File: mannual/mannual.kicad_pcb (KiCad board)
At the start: 2 copper layers, 31 parts, among them J1 Conn_02x07_Odd_Even, J10 Conn_02x10_Odd_Even, J2 Conn_01x02, J3 Conn_01x02, J4 Conn_01x02, J5 Conn_01x02, J6 Conn_01x02, J7 Conn_01x02, J8 Conn_01x02, J9 Conn_02x10_Odd_Even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

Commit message: modified the automatic circuit
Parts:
- moved J1 41.3 mm to (82.6, 109.4)
- moved Q6 41.3 mm to (106.2, 95.4)
- moved R1 41.3 mm to (109.8, 99.3)
- moved R5 41.3 mm to (109.9, 109.8)
- moved R8 41.3 mm to (101.4, 107.1)
- moved R9 41.3 mm to (79.2, 109.2)
- moved J10 41.3 mm to (123.4, 83.8)
- moved J2 41.3 mm to (117.0, 97.6)
- moved J3 41.3 mm to (117.0, 108.1)
- moved J4 41.3 mm to (87.0, 84.1)
- moved J7 41.3 mm to (118.3, 84.1)
- moved J8 41.3 mm to (76.6, 84.1)
- moved J9 41.3 mm to (64.0, 83.9)
- moved Q2 41.3 mm to (72.0, 95.3)
- moved Q3 41.3 mm to (80.9, 95.4)
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
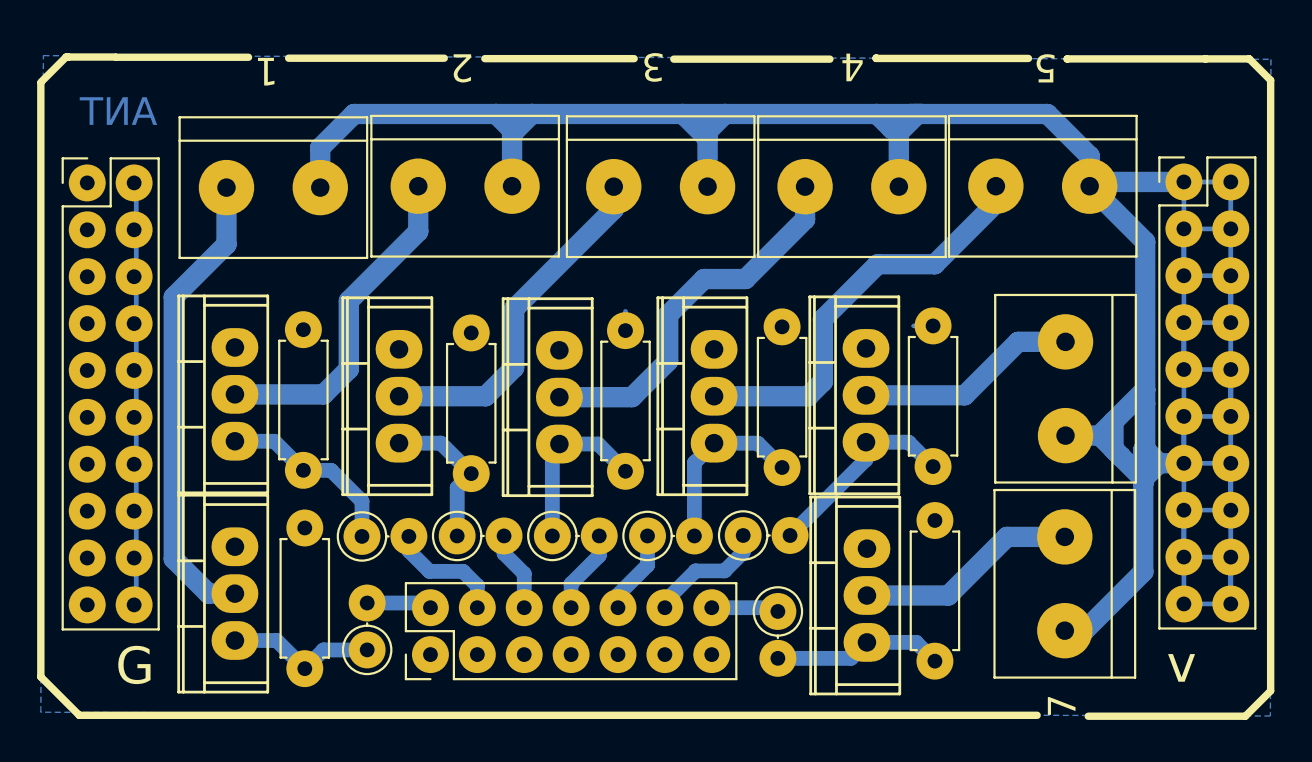
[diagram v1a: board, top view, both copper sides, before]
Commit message: Buck circuit also modified and pdfs also changed
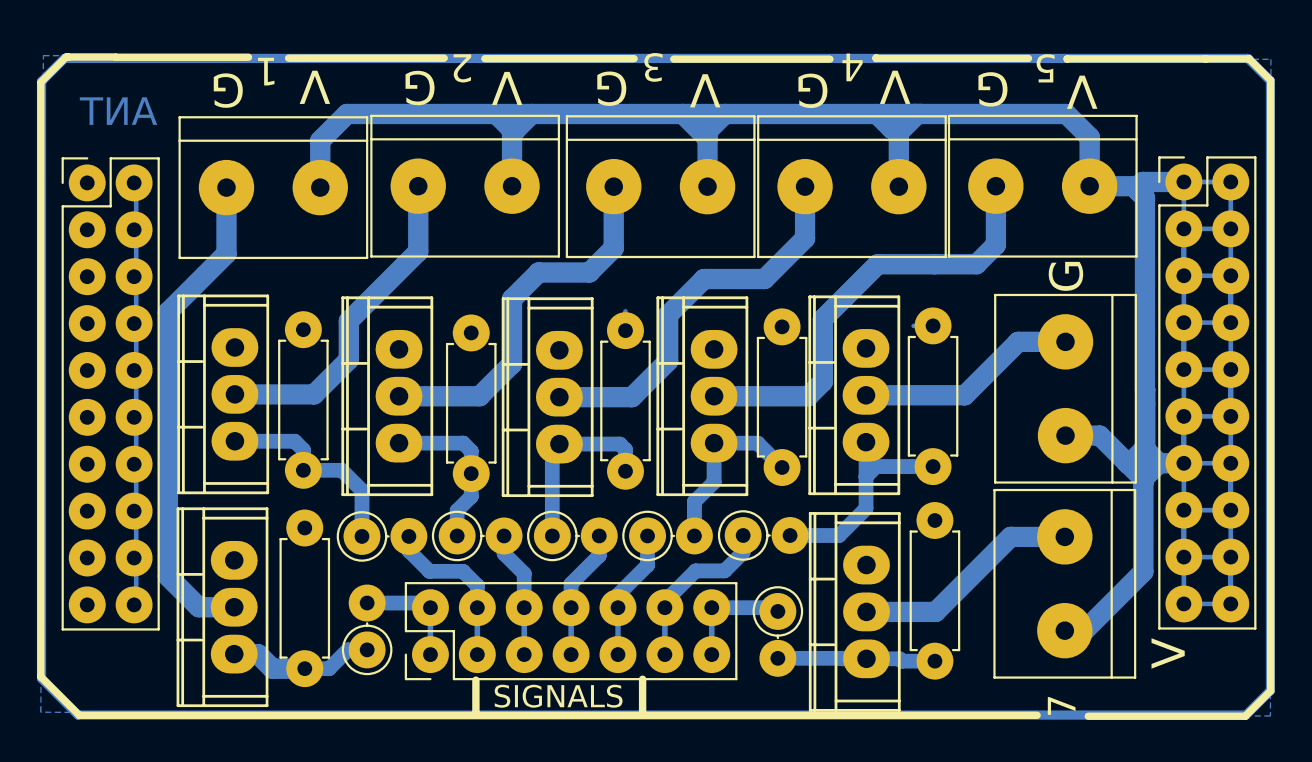
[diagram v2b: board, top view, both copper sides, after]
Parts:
- moved Q7 0.89 mm to (106.2, 107.1)
- moved Q1 0.74 mm to (72.0, 106.9)
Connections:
- J1 pad 12: Net-(J1-Pad12) -> Net-(J1-Pad11)
- J1 pad 14: Net-(J1-Pad14) -> Net-(J1-Pad13)
- J1 pad 2: Net-(J1-Pad2) -> Net-(J1-Pad1)
- J1 pad 4: Net-(J1-Pad4) -> Net-(J1-Pad3)
- J1 pad 6: Net-(J1-Pad6) -> Net-(J1-Pad5)
- J1 pad 8: Net-(J1-Pad8) -> Net-(J1-Pad7)
- J1 pad 9: Net-(J1-Pad9) -> Net-(J1-Pad10)
- R10 pad 2: Net-(J1-Pad4) -> Net-(J1-Pad3)
- R11 pad 1: Net-(J1-Pad12) -> Net-(J1-Pad11)
- R12 pad 2: Net-(J1-Pad6) -> Net-(J1-Pad5)
- R13 pad 2: Net-(J1-Pad8) -> Net-(J1-Pad7)
- R8 pad 1: Net-(J1-Pad14) -> Net-(J1-Pad13)
- R9 pad 2: Net-(J1-Pad2) -> Net-(J1-Pad1)
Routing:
- net (no net): track 0.00 -> 200.9 mm
- net Net-(J1-Pad11): track 0.00 -> 9.13 mm
- net Net-(J1-Pad3): track 0.00 -> 9.00 mm
- net Net-(J1-Pad7): track 0.00 -> 7.06 mm
- net Net-(J1-Pad5): track 0.00 -> 6.88 mm
- net Net-(J1-Pad12): track 6.59 -> 0.00 mm
- net Net-(J1-Pad4): track 6.46 -> 0.00 mm
- net Net-(J1-Pad13): track 0.00 -> 6.21 mm
- net Net-(J1-Pad1): track 0.00 -> 6.07 mm
- net +12V: track 218.6 -> 213.7 mm
- net Net-(J1-Pad8): track 4.52 -> 0.00 mm
- net Net-(J1-Pad6): track 4.34 -> 0.00 mm
- net Net-(J1-Pad14): track 3.67 -> 0.00 mm
- net Net-(J1-Pad2): track 3.53 -> 0.00 mm
- net Net-(J5-Pad2): track 18.9 -> 21.6 mm
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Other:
- board text added: "SIGNALS"
- board text added: "V"
- board text removed: "v"
